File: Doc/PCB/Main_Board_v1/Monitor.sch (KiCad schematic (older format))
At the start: 50 parts, among them J1 TE_3.5mm_Screwless_P2, J14 Button_LED, J15 Button, J2 TE_3.5mm_Screwless_P2, J3 UART_M, J4 Conn_01x08, J5 BUZZER, J6 I2C Interface LCD_M, Q1 IRLZ34N, U1 LM358, U2 LM7805_TO220, U3 XPRESS-40

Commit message: First placement of board
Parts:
- added R33, R34: 470, Resistor_THT:R_Axial_DIN0207_L6.3mm_D2.5mm_P10.16mm_Horizontal, symbol Device:R
- added R35: 10k, Resistor_THT:R_Axial_DIN0207_L6.3mm_D2.5mm_P10.16mm_Horizontal, symbol Device:R
- added TP9: TestPoint_Alt, Ventilator:pcb, symbol Connector:TestPoint_Alt
- C1, C11, C12, C13, C21, C7, C8, C9: value 100nF -> 100nF - 100V; footprint Capacitor_THT:C_Rect_L9.0mm_W3.3mm_P7.50mm_MKT -> Capacitor_THT:C_Rect_L7.2mm_W2.5mm_P5.00mm_FKS2_FKP2_MKS2_MKP2
- C10, C2, C20, C3, C4, C6: footprint Capacitor_THT:C_Rect_L7.0mm_W2.5mm_P5.00mm -> Capacitor_THT:C_Rect_L13.0mm_W4.0mm_P10.00mm_FKS3_FKP3_MKS4
- C5: footprint Capacitor_THT:CP_Radial_D5.0mm_P2.50mm -> Capacitor_THT:CP_Radial_D5.0mm_P2.00mm
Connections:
- net +5V_M: now also R33.1, R34.1, R35.1
- net SCL: now also R33.2
- net SDA: now also R34.2
- net nMCLR renamed nMCLR_M
- net nMCLR_M: now also R35.2
- no-connect marks 22 -> 23

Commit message: Update in PCB: Schematic and Layout
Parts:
- J14: value Button_LED -> MUTE
- J15: value Button -> HISTORY
- MK1: footprint Connector_PinHeader_2.54mm:PinHeader_1x02_P2.54mm_Vertical -> Ventilator:MIC
- Q1: value IRLZ34N -> STP24NF10
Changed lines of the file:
@@
 F 0 "MK1" H 1030 6446 50  0000 L CNN
 F 1 "Microphone" H 1030 6355 50  0000 L CNN
-F 2 "Connector_PinHeader_2.54mm:PinHeader_1x02_P2.54mm_Vertical" V 900 6500 50  0001 C CNN
-F 3 "~" V 900 6500 50  0001 C CNN
+F 2 "Ventilator:MIC" V 900 6500 50  0001 C CNN
+F 3 "https://es.rs-online.com/web/p/componentes-de-microfono-para-condensador/7243125/?relevancy-data=636F3D3126696E3D4931384E525353746F636B4E756D626572266C753D656E266D6D3D6D61746368616C6C26706D3D5E2828282872737C5253295B205D3F293F285C647B337D5B5C2D5C735D3F5C647B332C347D5B705061415D3F29297C283235285C647B387D7C5C647B317D5C2D5C647B377D2929292426706F3D3126736E3D592673723D2673743D52535F53544F434B5F4E554D4245522677633D4E4F4E45267573743D3732342D33313235267374613D3732343331323526&searchHistory=%7B%22enabled%22%3Atrue%7D" V 900 6500 50  0001 C CNN
 	1    900  6400
 	1    0    0    -1
@@
 AR Path="/5E9337AC/5EB073C5" Ref="Q1"  Part="1"
 F 0 "Q1" H 2054 4696 50  0000 L CNN
-F 1 "IRLZ34N" H 2054 4605 50  0000 L CNN
+F 1 "STP24NF10 " H 2054 4605 50  0000 L CNN
 F 2 "Package_TO_SOT_THT:TO-220-3_Vertical" H 2100 4575 50  0001 L CIN
-F 3 "http://www.infineon.com/dgdl/irlz34npbf.pdf?fileId=5546d462533600a40153567206892720" H 1850 4650 50  0001 L CNN
+F 3 "https://es.rs-online.com/web/p/mosfet/6875377/" H 1850 4650 50  0001 L CNN
 	1    1850 4650
 	-1   0    0    -1
@@
 P 10550 2950
 F 0 "J14" H 10878 3001 50  0000 L CNN
-F 1 "Button_LED" H 10878 2910 50  0000 L CNN
+F 1 "MUTE" H 10878 2910 50  0000 L CNN
 F 2 "Ventilator:PushButton_LED" H 10550 2950 50  0001 C CNN
 F 3 "" H 10550 2950 50  0001 C CNN
@@
 P 10550 3350
 F 0 "J15" H 10878 3396 50  0000 L CNN
-F 1 "Button" H 10878 3305 50  0000 L CNN
+F 1 "HISTORY" H 10878 3305 50  0000 L CNN
 F 2 "Ventilator:PushButton" H 10550 3350 50  0001 C CNN
-F 3 "" H 10550 3350 50  0001 C CNN
+F 3 "https://es.rs-online.com/web/p/botones-pulsadores/7346827/" H 10550 3350 50  0001 C CNN
 	1    10550 3350
 	1    0    0    -1

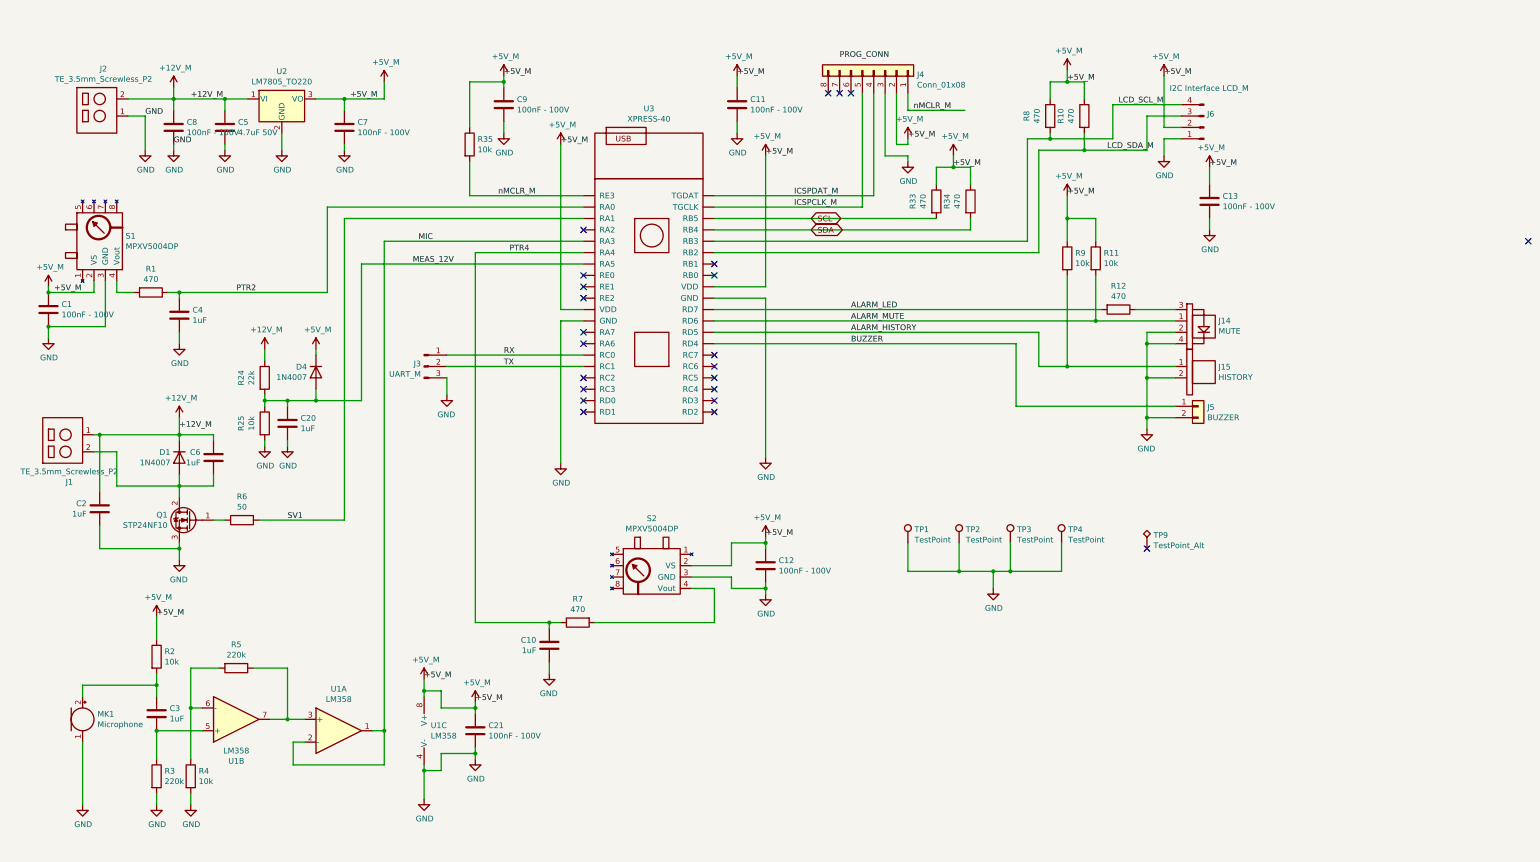
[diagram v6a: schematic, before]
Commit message: New PCB version; I2C Slave works
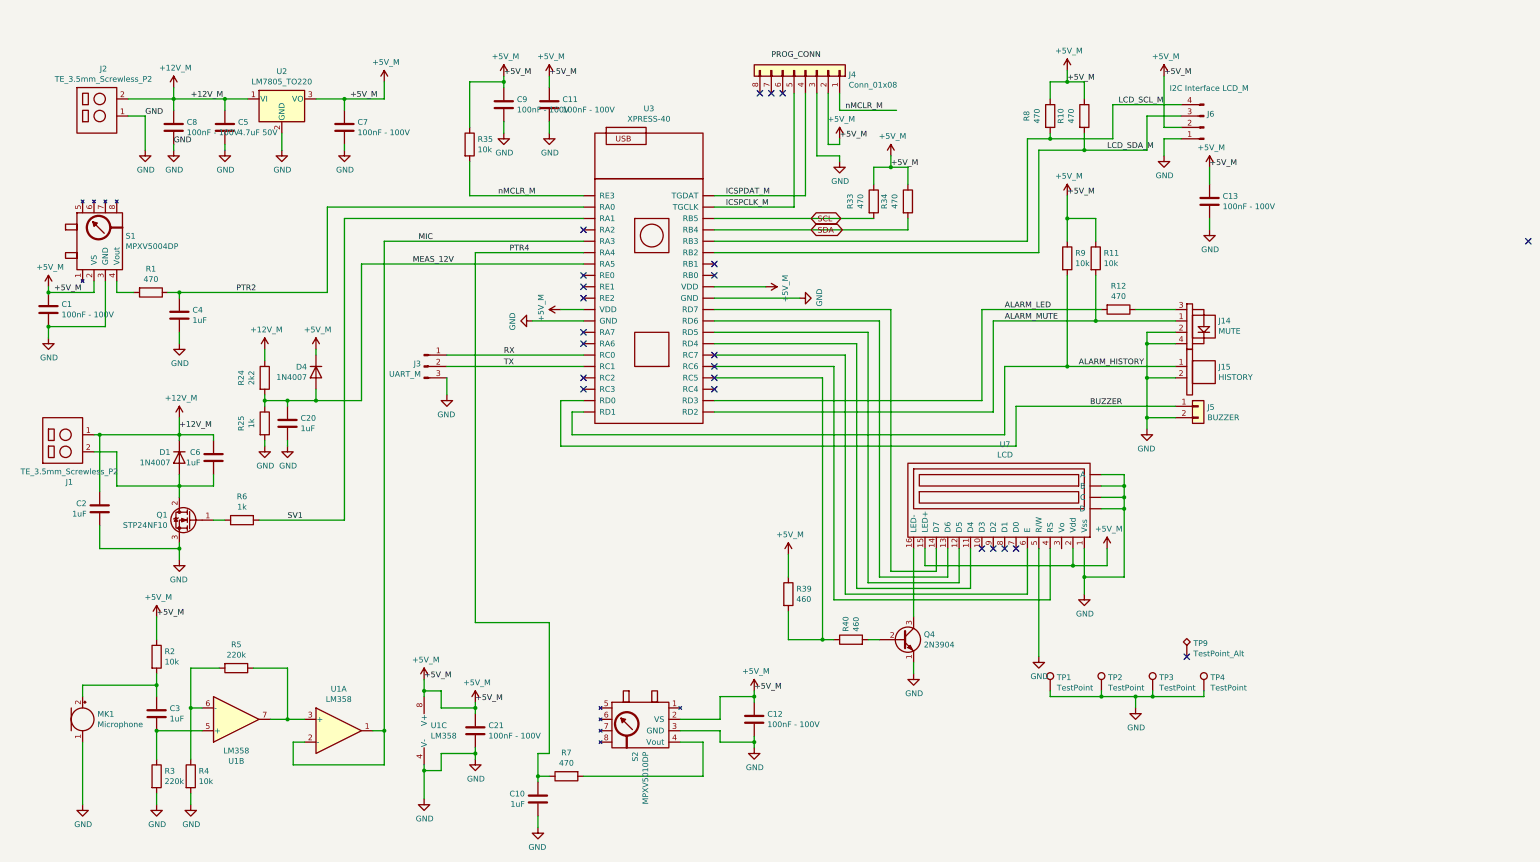
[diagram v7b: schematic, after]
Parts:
- removed S2: MPXV5004DP, Ventilator:1351-01, symbol Ventilator:MPXV5004DP
- added Q4: 2N3904, Package_TO_SOT_THT:TO-92_Inline, symbol Transistor_BJT:2N3904
- added R39, R40: 460, Resistor_THT:R_Axial_DIN0207_L6.3mm_D2.5mm_P10.16mm_Horizontal, symbol Device:R
- added S2: MPXV5010DP, Ventilator:1351-01, symbol Ventilator:MPXV5010DP
- added U7: LCD, Ventilator:LCD_2x16, symbol Ventilator:LCD
- R24: value 22k -> 2k2
- R25: value 10k -> 1k
- R6: value 50 -> 1k
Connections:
- net +5V_M: now also R39.1, S2.2 (VS), U7.15 (LED+), U7.2 (Vdd)
- net ALARM_HISTORY: now also U3.20 (RD1); no longer U3.28 (RD5)
- net ALARM_LED: now also U3.22 (RD3); no longer U3.30 (RD7)
- net ALARM_MUTE: now also U3.21 (RD2); no longer U3.29 (RD6)
- net BUZZER: now also U3.19 (RD0); no longer U3.27 (RD4)
- net GND: now also Q4.1 (E), S2.3 (GND), U7.1 (Vss), U7.5 (R/W), U7.~ (D)
- net at R7.2: now also S2.4 (Vout)
- net at U3.24 (RC5): now also R39.2, R40.1
- net at U3.25 (RC6): now also U7.4 (RS)
- net at U3.26 (RC7): now also U7.6 (E)
- new net: U3.27 (RD4), U7.11 (D4)
- new net: U3.28 (RD5), U7.12 (D5)
- new net: U3.29 (RD6), U7.13 (D6)
- new net: U3.30 (RD7), U7.14 (D7)
- new net: Q4.3 (C), U7.16 (LED-)
- new net: Q4.2 (B), R40.2
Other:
- moved on the sheet: C10, C11, C12, J4, R33, R34, R7, TP1, TP2, TP3, TP4, TP9

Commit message: New V1 placement done. Speed up Monitor to 64 MHz
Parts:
- removed TP9: TestPoint_Alt, Ventilator:pcb, symbol Connector:TestPoint_Alt
- added RV1: 1K, Ventilator:Potentiometer_409HA, symbol Device:R_POT
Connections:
- net +5V_M: now also RV1.1
- net GND: now also RV1.3
- net at U7.3 (Vo): now also RV1.2
- no-connect marks 23 -> 20
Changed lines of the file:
@@
 Wire Wire Line
 	3050 1900 5300 1900
-NoConn ~ 6450 3200
-NoConn ~ 6450 3300
-NoConn ~ 6450 3400
 NoConn ~ 5300 2500
 NoConn ~ 5300 2600
@@
 Wire Wire Line
 	9850 6200 10150 6200
-$Comp
-L Connector:TestPoint_Alt TP9
-U 1 1 5F26F9EB
-P 10600 5850
-F 0 "TP9" H 10658 5968 50  0000 L CNN
-F 1 "TestPoint_Alt" H 10658 5877 50  0000 L CNN
-F 2 "Ventilator:pcb" H 10800 5850 50  0001 C CNN
-F 3 "~" H 10800 5850 50  0001 C CNN
-	1    10600 5850
-	1    0    0    -1
-$EndComp
 NoConn ~ 10600 5850
 Wire Wire Line
@@
 	9200 5300 9200 4900
 Wire Wire Line
-	9300 4900 9300 5850
+	9300 4900 9300 5750
 Wire Wire Line
 	9400 4900 9400 5350
@@
 	8300 4900 8300 5050
 Wire Wire Line
-	8300 5050 9600 5050
+	8300 5050 8950 5050
 Connection ~ 9600 5050
 Wire Wire Line
@@
 Wire Wire Line
 	7400 5700 7500 5700
+$Comp
+L Device:R_POT RV1
+U 1 1 5EA73AB9
+P 8950 5550
+F 0 "RV1" H 8880 5596 50  0000 R CNN
+F 1 "1K" H 8880 5505 50  0000 R CNN
+F 2 "Ventilator:Potentiometer_409HA" H 8950 5550 50  0001 C CNN
+F 3 "https://es.rs-online.com/web/p/resistencias-variables/6524546/" H 8950 5550 50  0001 C CNN
+	1    8950 5550
+	1    0    0    -1
+$EndComp
+Wire Wire Line
+	8950 5400 8950 5050
+Connection ~ 8950 5050
+Wire Wire Line
+	8950 5050 9600 5050
+Wire Wire Line
+	8950 5700 8950 5750
+Wire Wire Line
+	8950 5750 9300 5750
+Connection ~ 9300 5750
+Wire Wire Line
+	9300 5750 9300 5850
+Wire Wire Line
+	9500 4900 9500 5550
+Wire Wire Line
+	9500 5550 9100 5550
 $EndSCHEMATC
